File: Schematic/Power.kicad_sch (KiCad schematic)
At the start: 42 parts, among them IC1 MP9943AGQ-Z, IC2 MP9943AGQ-Z, U2 ME6217C33M5G, U3 LDO-1.8v

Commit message: Refactor code structure for improved readability and maintainability
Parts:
- removed IC1, IC2: MP9943AGQ-Z, fch7_fp:SON65P300X300X100-8N, symbol MP9943AGQ-Z:MP9943AGQ-Z
- removed U2: ME6217C33M5G, fch7_fp:SOT23-5, symbol ME6217C33M5G:ME6217C33M5G
- removed U3: LDO-1.8v, fch7_fp:AP2112K-1.8TRG1, symbol fch7_sym:AP2112K-1.8TRG1
- added IC1, IC2: MP9943AGQ-Z, fch7_fp:SON65P300X300X100-8N, symbol fclib:MP9943AGQ-Z
- added U2: ME6217C33M5G, fch7_fp:SOT23-5, symbol fclib:ME6217C33M5G
- added U3: LDO-1.8v, fch7_fp:AP2112K-1.8TRG1, symbol fclib:AP2112K-1.8TRG1
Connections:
- net 4V5: now also U2.1 (IN), U2.3 (CE), U3.1 (VIN)
- net FB_5V: now also IC2.1 (FB)
- net FB_9V: now also IC1.1 (FB)
- net GND: now also IC1.5 (GND), IC2.5 (GND), U2.2 (GND), U3.2 (GND)
- net LC_5V: now also IC2.6 (SW)
- net LC_9V: now also IC1.6 (SW)
- net VBAT: now also IC1.7 (IN), IC2.7 (IN)
- net VCC_ICM: now also U3.5 (VOUT)
- net VDD_MCU: now also U2.5 (OUT)
- net at C16.2, R10.1: now also IC2.2 (VCC)
- net at R11.2: now also IC2.3 (EN/SYNC)
- net at C17.2: now also IC2.4 (BST)
- net at R10.2: now also IC2.8 (PG)
- net at C20.2, R14.1: now also IC1.2 (VCC)
- net at R14.2: now also IC1.8 (PG)
- net at C21.2: now also IC1.4 (BST)
- net at R13.2: now also IC1.3 (EN/SYNC)

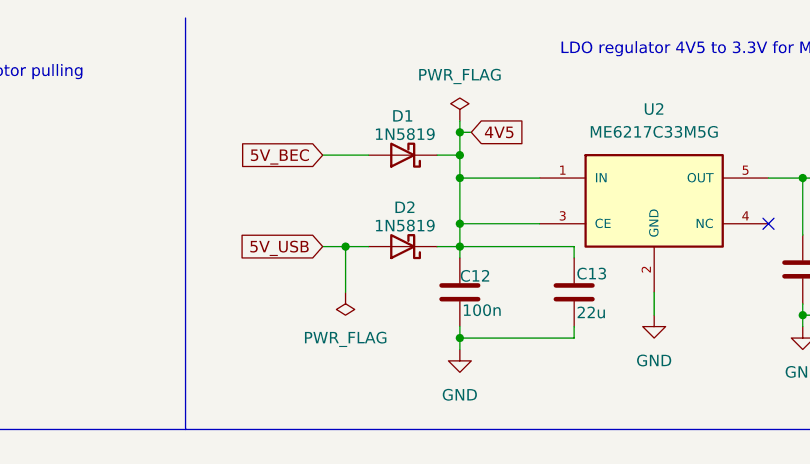
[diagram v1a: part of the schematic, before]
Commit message: Update fp-info-cache with new component values and add SOD-123 and SOD-323 footprints
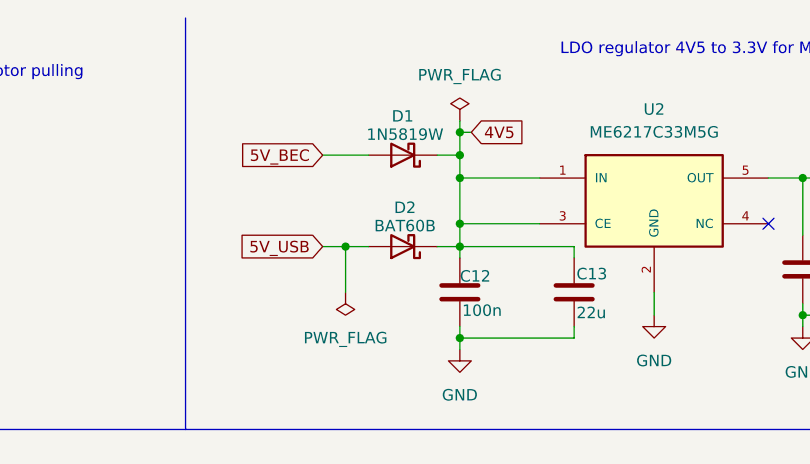
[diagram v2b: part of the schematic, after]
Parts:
- D1: value 1N5819 -> 1N5819W; footprint Diode_THT:D_DO-41_SOD81_P10.16mm_Horizontal -> fch7_fp:SOD-123_L2.7-W1.6-LS3.7-RD; MPN 1N5819 -> 1N5819W; Manufacturer STM -> JSMSEMI
- D2: value 1N5819 -> BAT60B; footprint Diode_THT:D_DO-41_SOD81_P10.16mm_Horizontal -> fch7_fp:SOD-323_L1.8-W1.3-LS2.5-RD; MPN 1N5819 -> BAT60B; Manufacturer STM -> JSCJ
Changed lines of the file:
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@@
 			)
 		)
-		(property "Value" "1N5819"
+		(property "Value" "1N5819W"
 			(at 133.604 25.654 0)
 			(effects
@@
 			)
 		)
-		(property "Footprint" "Diode_THT:D_DO-41_SOD81_P10.16mm_Horizontal"
+		(property "Footprint" "fch7_fp:SOD-123_L2.7-W1.6-LS3.7-RD"
 			(at 133.35 23.495 0)
 			(effects
@@
 			)
 		)
-		(property "Datasheet" "http://www.vishay.com/docs/88525/1n5817.pdf"
+		(property "Datasheet" "https://www.lcsc.com/datasheet/C963381.pdf"
 			(at 133.35 27.94 0)
 			(effects
@@
 			)
 		)
-		(property "MPN" "1N5819"
+		(property "MPN" "1N5819W"
 			(at 133.35 27.94 0)
 			(effects
@@
 			)
 		)
-		(property "Manufacturer" "STM"
+		(property "Manufacturer" "JSMSEMI"
 			(at 133.35 27.94 0)
 			(effects
@@
 			)
 		)
-		(property "Value" "1N5819"
+		(property "Value" "BAT60B"
 			(at 133.604 35.814 0)
 			(effects
@@
 			)
 		)
-		(property "Footprint" "Diode_THT:D_DO-41_SOD81_P10.16mm_Horizontal"
+		(property "Footprint" "fch7_fp:SOD-323_L1.8-W1.3-LS2.5-RD"
 			(at 133.35 33.655 0)
 			(effects
@@
 			)
 		)
-		(property "MPN" "1N5819"
+		(property "MPN" "BAT60B"
 			(at 133.35 38.1 0)
 			(effects
@@
 			)
 		)
-		(property "Manufacturer" "STM"
+		(property "Manufacturer" "JSCJ"
 			(at 133.35 38.1 0)
 			(effects

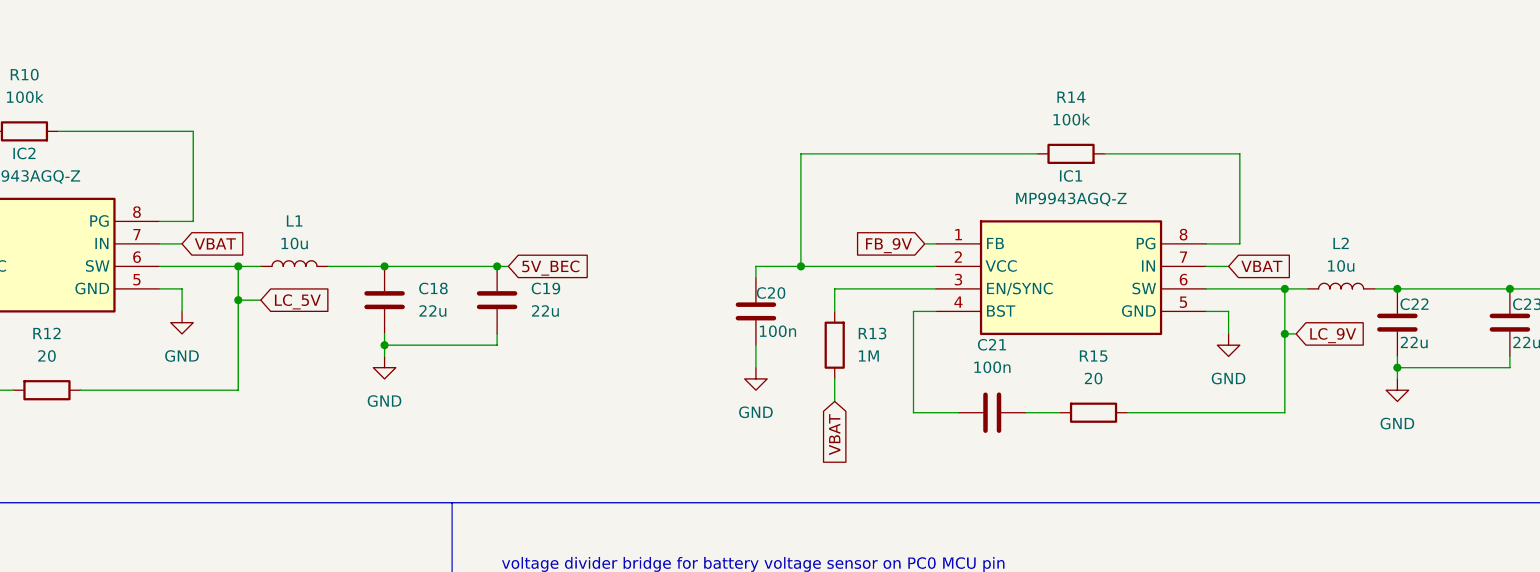
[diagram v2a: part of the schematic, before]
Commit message: Refactor schematic files and add net definitions
- Updated priority values for GND and POWER net classes in fch7.kicad_pro.
- Added USB_DIFF net class with associated patterns for USB differential signals.
- Removed duplicate junctions and adjusted wire connections in rf_rx.kicad_sch for clarity.
- Adjusted component positions and properties in rf_rx.kicad_sch for better layout.
- Modified text positions for IMU components in sensors.kicad_sch to improve readability.
- Cleaned up unnecessary wires and added new connections in sensors.kicad_sch.
- Introduced nets.txt file to define various electrical nets used across the schematics.
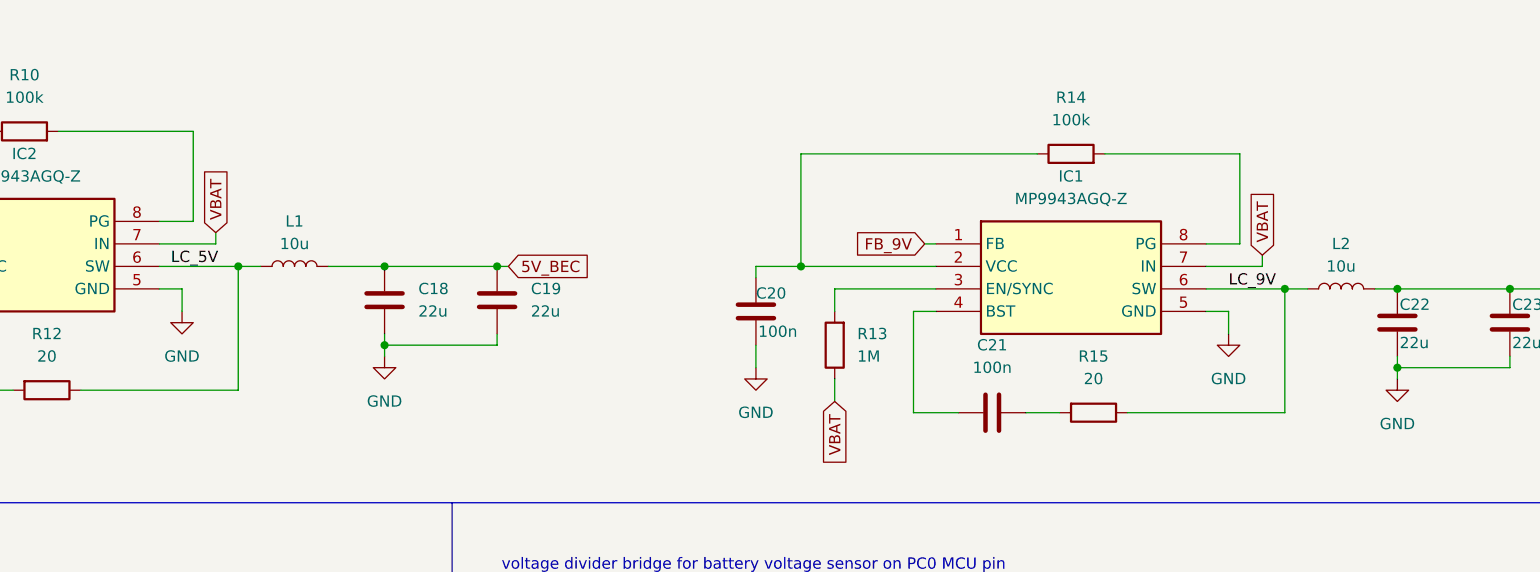
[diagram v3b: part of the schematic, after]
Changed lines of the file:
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@@
-	)
-	(junction
-		(at 212.09 113.03)
-		(diameter 0)
-		(color 0 0 0 0)
 	)
 	(junction
@@
 	(junction
 		(at 39.37 162.56)
-		(diameter 0)
-		(color 0 0 0 0)
-	)
-	(junction
-		(at 93.98 109.22)
 		(diameter 0)
 		(color 0 0 0 0)
@@
 	(wire
 		(pts
-			(xy 93.98 109.22) (xy 93.98 105.41)
+			(xy 93.98 105.41) (xy 93.98 119.38)
 		)
 		(stroke
@@
 	(wire
 		(pts
+			(xy 91.44 101.6) (xy 91.44 102.87)
+		)
+		(stroke
+			(width 0)
+			(type default)
+		)
+	)
+	(wire
+		(pts
 			(xy 152.4 105.41) (xy 152.4 106.68)
 		)
@@
 	(wire
 		(pts
-			(xy 93.98 109.22) (xy 96.52 109.22)
-		)
-		(stroke
-			(width 0)
-			(type default)
-		)
-	)
-	(wire
-		(pts
 			(xy 93.98 105.41) (xy 96.52 105.41)
 		)
@@
 	(wire
 		(pts
-			(xy 212.09 121.92) (xy 212.09 113.03)
-		)
-		(stroke
-			(width 0)
-			(type default)
-		)
-	)
-	(wire
-		(pts
 			(xy 139.7 30.48) (xy 139.7 35.56)
 		)
@@
 	(wire
 		(pts
-			(xy 212.09 113.03) (xy 212.09 107.95)
+			(xy 212.09 107.95) (xy 212.09 121.92)
 		)
 		(stroke
@@
 	(wire
 		(pts
-			(xy 85.09 102.87) (xy 87.63 102.87)
+			(xy 85.09 102.87) (xy 91.44 102.87)
 		)
 		(stroke
@@
 	(wire
 		(pts
-			(xy 203.2 105.41) (xy 205.74 105.41)
+			(xy 203.2 105.41) (xy 209.55 105.41)
 		)
 		(stroke
@@
 	(wire
 		(pts
-			(xy 212.09 113.03) (xy 213.36 113.03)
-		)
-		(stroke
-			(width 0)
-			(type default)
-		)
-	)
-	(wire
-		(pts
 			(xy 39.37 162.56) (xy 40.64 162.56)
 		)
@@
 	(wire
 		(pts
+			(xy 209.55 105.41) (xy 209.55 104.14)
+		)
+		(stroke
+			(width 0)
+			(type default)
+		)
+	)
+	(wire
+		(pts
 			(xy 140.97 173.99) (xy 140.97 175.26)
 		)
@@
 	(wire
 		(pts
-			(xy 93.98 119.38) (xy 93.98 109.22)
-		)
-		(stroke
-			(width 0)
-			(type default)
-		)
-	)
-	(wire
-		(pts
 			(xy 152.4 46.99) (xy 152.4 48.26)
 		)
@@
 			(width 0)
 			(type default)
+		)
+	)
+	(label "LC_5V"
+		(at 86.36 105.41 0)
+		(effects
+			(font
+				(size 1.27 1.27)
+			)
+			(justify left bottom)
+		)
+	)
+	(label "LC_9V"
+		(at 205.74 107.95 0)
+		(effects
+			(font
+				(size 1.27 1.27)
+			)
+			(justify left bottom)
 		)
 	)
@@
 	(global_label "VBAT"
 		(shape input)
-		(at 87.63 102.87 0)
+		(at 91.44 101.6 90)
 		(fields_autoplaced yes)
 		(effects
@@
 		)
 		(property "Intersheetrefs" "${INTERSHEET_REFS}"
-			(at 95.03 102.87 0)
+			(at 91.44 94.2 90)
 			(effects
 				(font
@@
 	(global_label "VBAT"
 		(shape input)
-		(at 205.74 105.41 0)
+		(at 209.55 104.14 90)
 		(fields_autoplaced yes)
 		(effects
@@
 		)
 		(property "Intersheetrefs" "${INTERSHEET_REFS}"
-			(at 213.14 105.41 0)
-			(effects
-				(font
-					(size 1.27 1.27)
-				)
-				(justify left)
-				(hide yes)
-			)
-		)
-	)
-	(global_label "LC_5V"
-		(shape input)
-		(at 96.52 109.22 0)
-		(fields_autoplaced yes)
-		(effects
-			(font
-				(size 1.27 1.27)
-			)
-			(justify left)
-		)
-		(property "Intersheetrefs" "${INTERSHEET_REFS}"
-			(at 105.069 109.22 0)
+			(at 209.55 96.74 90)
 			(effects
 				(font
@@
 			(effects
 				(font
-					(size 1.27 1.27)
-				)
-				(justify left)
-				(hide yes)
-			)
-		)
-	)
-	(global_label "LC_9V"
-		(shape input)
-		(at 213.36 113.03 0)
-		(fields_autoplaced yes)
-		(effects
-			(font
-				(size 1.27 1.27)
-			)
-			(justify left)
-		)
-		(property "Intersheetrefs" "${INTERSHEET_REFS}"
-			(at 221.909 113.03 0)
-			(effects
-				(font

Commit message: finished every routing and fix errors in DRC
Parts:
- D1: footprint fch7_fp:SOD-123_L2.7-W1.6-LS3.7-RD -> fch7:SOD-123_L2.7-W1.6-LS3.7-RD
- D2: footprint fch7_fp:SOD-323_L1.8-W1.3-LS2.5-RD -> fch7:SOD-323_L1.8-W1.3-LS2.5-RD
- IC1, IC2: footprint fch7_fp:SON65P300X300X100-8N -> fch7:SON65P300X300X100-8N
- U2: footprint fch7_fp:SOT23-5 -> fch7:SOT23-5
- U3: footprint fch7_fp:AP2112K-1.8TRG1 -> fch7:AP2112K-1.8TRG1
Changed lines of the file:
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@@
 			)
 		)
-		(property "Footprint" "fch7_fp:AP2112K-1.8TRG1"
+		(property "Footprint" "fch7:AP2112K-1.8TRG1"
 			(at 237.998 24.638 0)
 			(effects
@@
 			)
 		)
-		(property "Footprint" "fch7_fp:SOD-123_L2.7-W1.6-LS3.7-RD"
+		(property "Footprint" "fch7:SOD-123_L2.7-W1.6-LS3.7-RD"
 			(at 133.35 23.495 0)
 			(effects
@@
 			)
 		)
-		(property "Footprint" "fch7_fp:SON65P300X300X100-8N"
+		(property "Footprint" "fch7:SON65P300X300X100-8N"
 			(at 81.28 195.25 0)
 			(effects
@@
 			)
 		)
-		(property "Footprint" "fch7_fp:SOT23-5"
+		(property "Footprint" "fch7:SOT23-5"
 			(at 161.29 33.02 0)
 			(effects
@@
 			)
 		)
-		(property "Footprint" "fch7_fp:SON65P300X300X100-8N"
+		(property "Footprint" "fch7:SON65P300X300X100-8N"
 			(at 199.39 197.79 0)
 			(effects
@@
 			)
 		)
-		(property "Footprint" "fch7_fp:SOD-323_L1.8-W1.3-LS2.5-RD"
+		(property "Footprint" "fch7:SOD-323_L1.8-W1.3-LS2.5-RD"
 			(at 133.35 33.655 0)
 			(effects

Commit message: Update schematic properties and model paths - Added MPN and Manufacturer properties for ICM-42688-P and MPU-6500 in sensors.kicad_sch. - Changed model paths to use the ${FCH7_3DMODEL_DIR} variable for various components in the fch7.pretty library. - Added a 3D model for the SOD-123 component.
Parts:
- IC1, IC2: MPN (none) -> MP9943AGQ-Z; Manufacturer (none) -> Monolithic Power Systems (MPS)
- U3: MPN (none) -> AP2112K-1.8TRG1
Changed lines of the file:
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@@
+			)
+		)
+		(property "MPN" "AP2112K-1.8TRG1"
+			(at 238.76 36.83 0)
+			(effects
+				(font
+					(size 1.27 1.27)
+				)
+				(hide yes)
 			)
 		)
@@
 			)
 		)
+		(property "MPN" "MP9943AGQ-Z"
+			(at 54.61 100.33 0)
+			(effects
+				(font
+					(size 1.27 1.27)
+				)
+				(hide yes)
+			)
+		)
+		(property "Manufacturer" "Monolithic Power Systems (MPS)"
+			(at 54.61 100.33 0)
+			(effects
+				(font
+					(size 1.27 1.27)
+				)
+				(hide yes)
+			)
+		)
 		(pin "1"
 		)
@@
 				(hide yes)
 			)
+		)
+		(property "MPN" "MP9943AGQ-Z"
+			(at 172.72 102.87 0)
+			(effects
+				(font
+					(size 1.27 1.27)
+				)
+				(hide yes)
+			)
+		)
+		(property "Manufacturer" "Monolithic Power Systems (MPS)"
+			(at 172.72 102.87 0)
+			(effects
+				(font
+					(size 1.27 1.27)
+				)
+				(hide yes)
+			)
